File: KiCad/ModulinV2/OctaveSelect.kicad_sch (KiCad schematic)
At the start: 53 parts, among them IC21 SN74LV10ADR, IC22 SN74LV10ADR, IC23 SN74LV10ADR, IC24 SN74HC193DR, IC25 TMUX4051DYYRQ1, IC26 CD4028BM96, Q3 BC847B,215, Q4 BC847B,215, Q5 BC847B,215, Q6 BC847B,215, Q7 BC847B,215

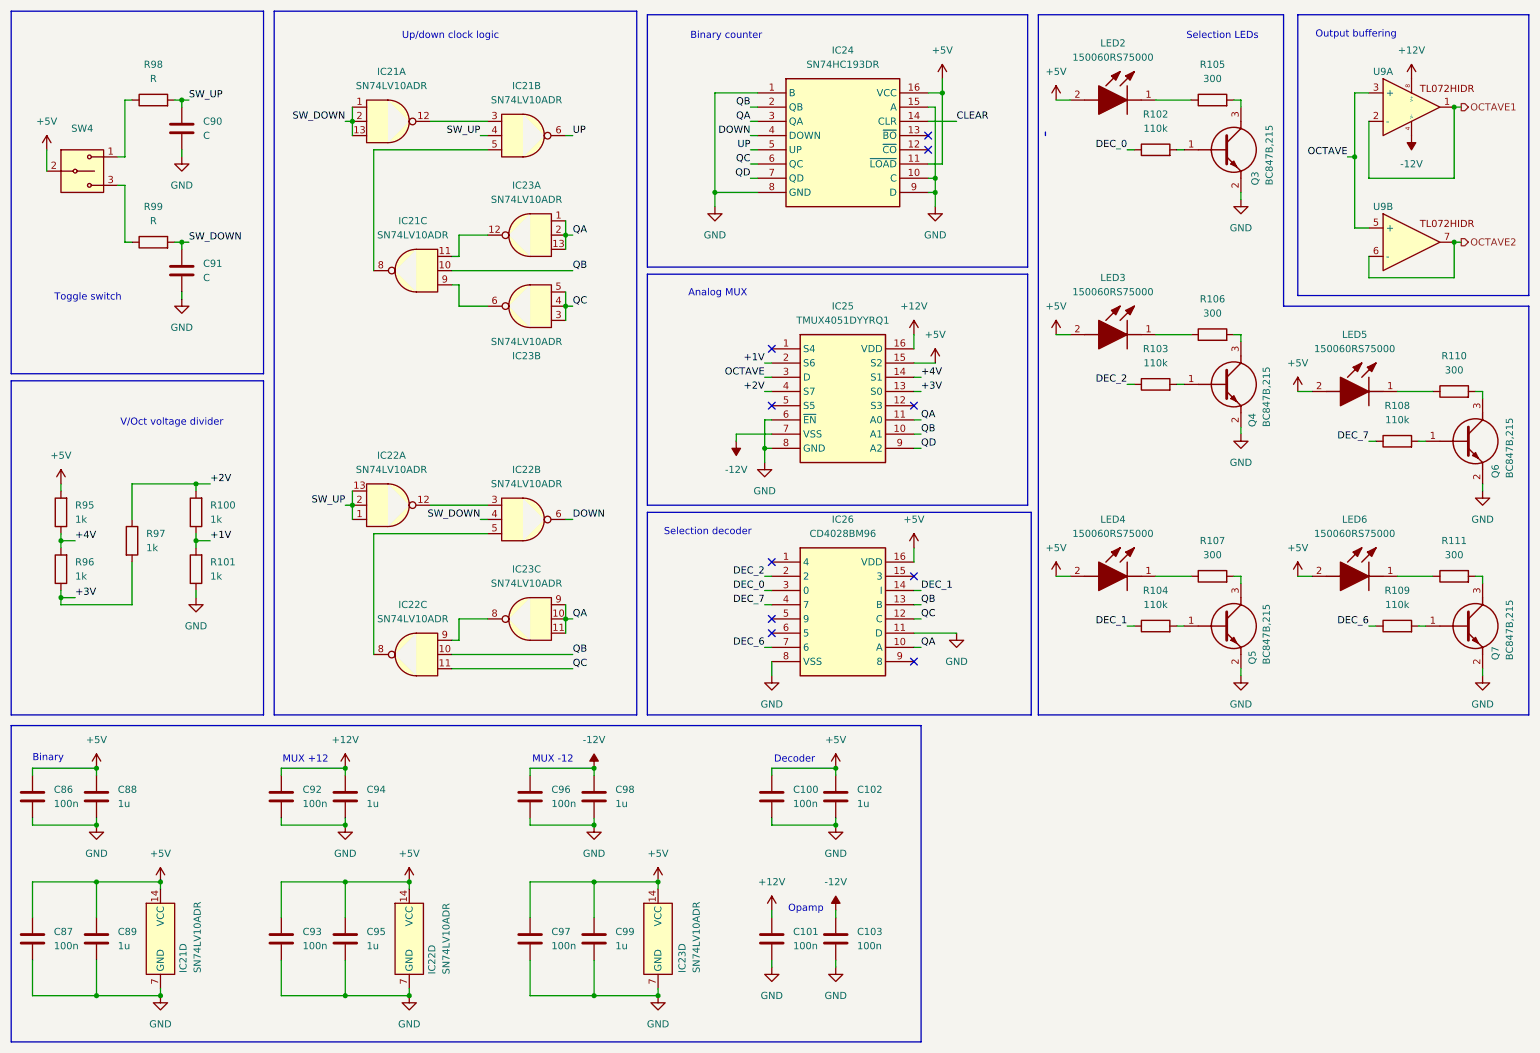
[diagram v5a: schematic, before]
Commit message: Added 4k7 pullups to I2C lines
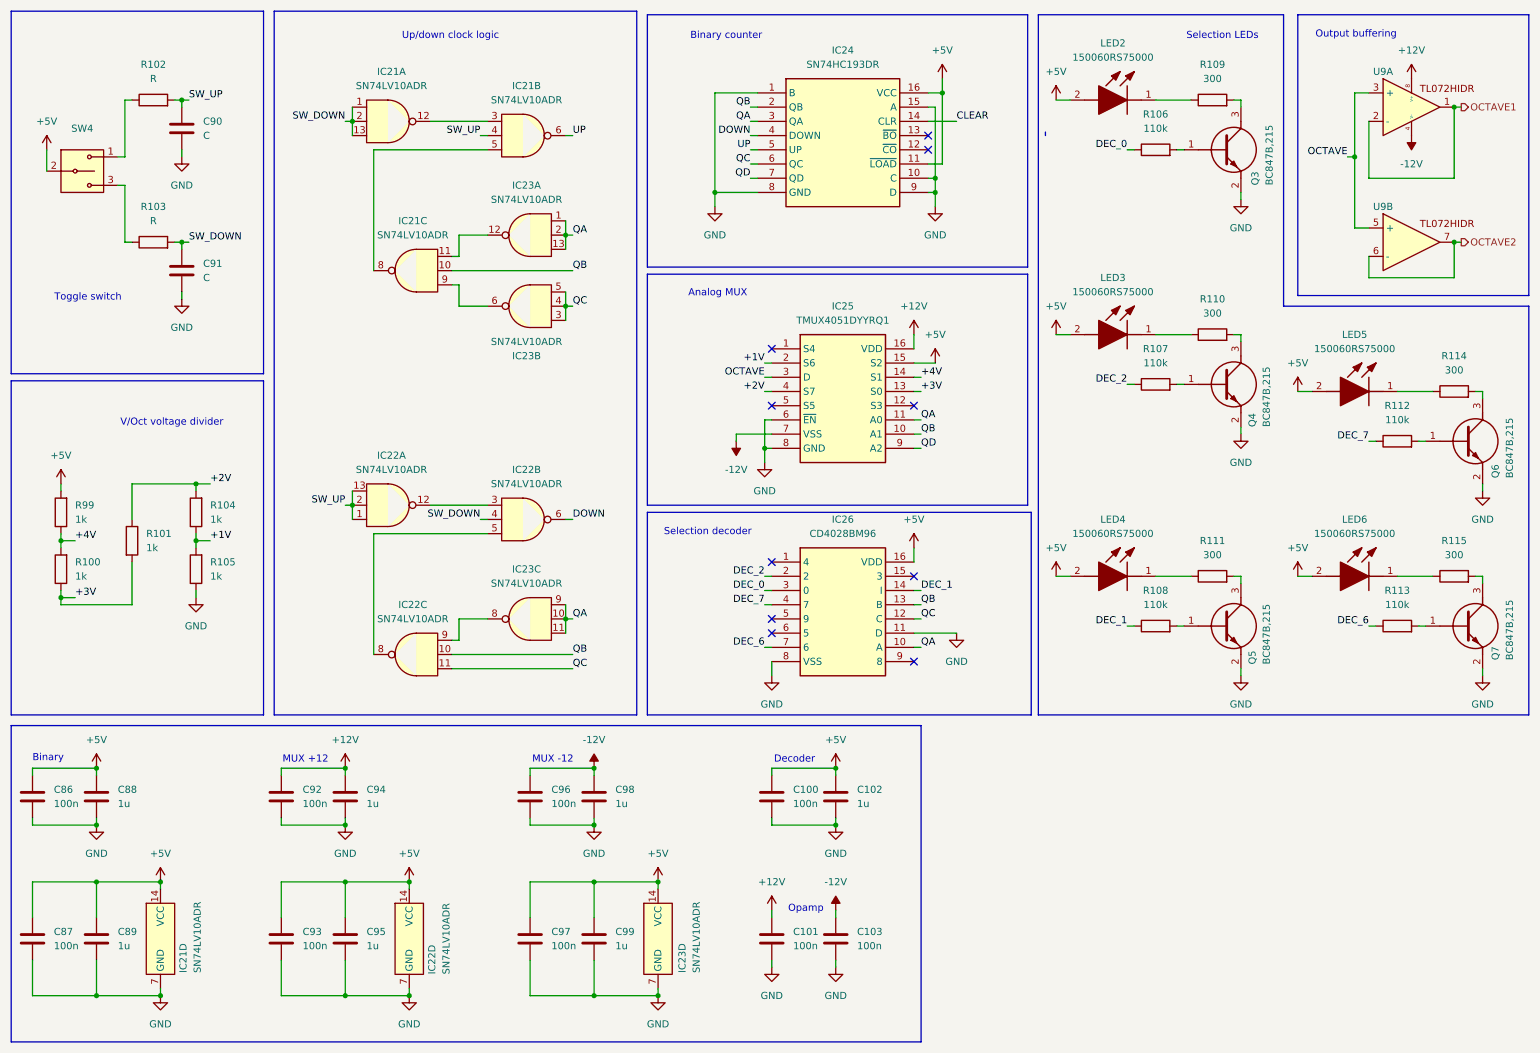
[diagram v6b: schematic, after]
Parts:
- renumbered R96 to R100, R97 to R101, R98 to R102, R99 to R103, R100 to R104, R101 to R105, R102 to R106, R103 to R107, R104 to R108, R105 to R109, R106 to R110, R107 to R111, R108 to R112, R109 to R113, R110 to R114, R111 to R115, R95 to R99

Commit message: Added wave selection jumpers for testing
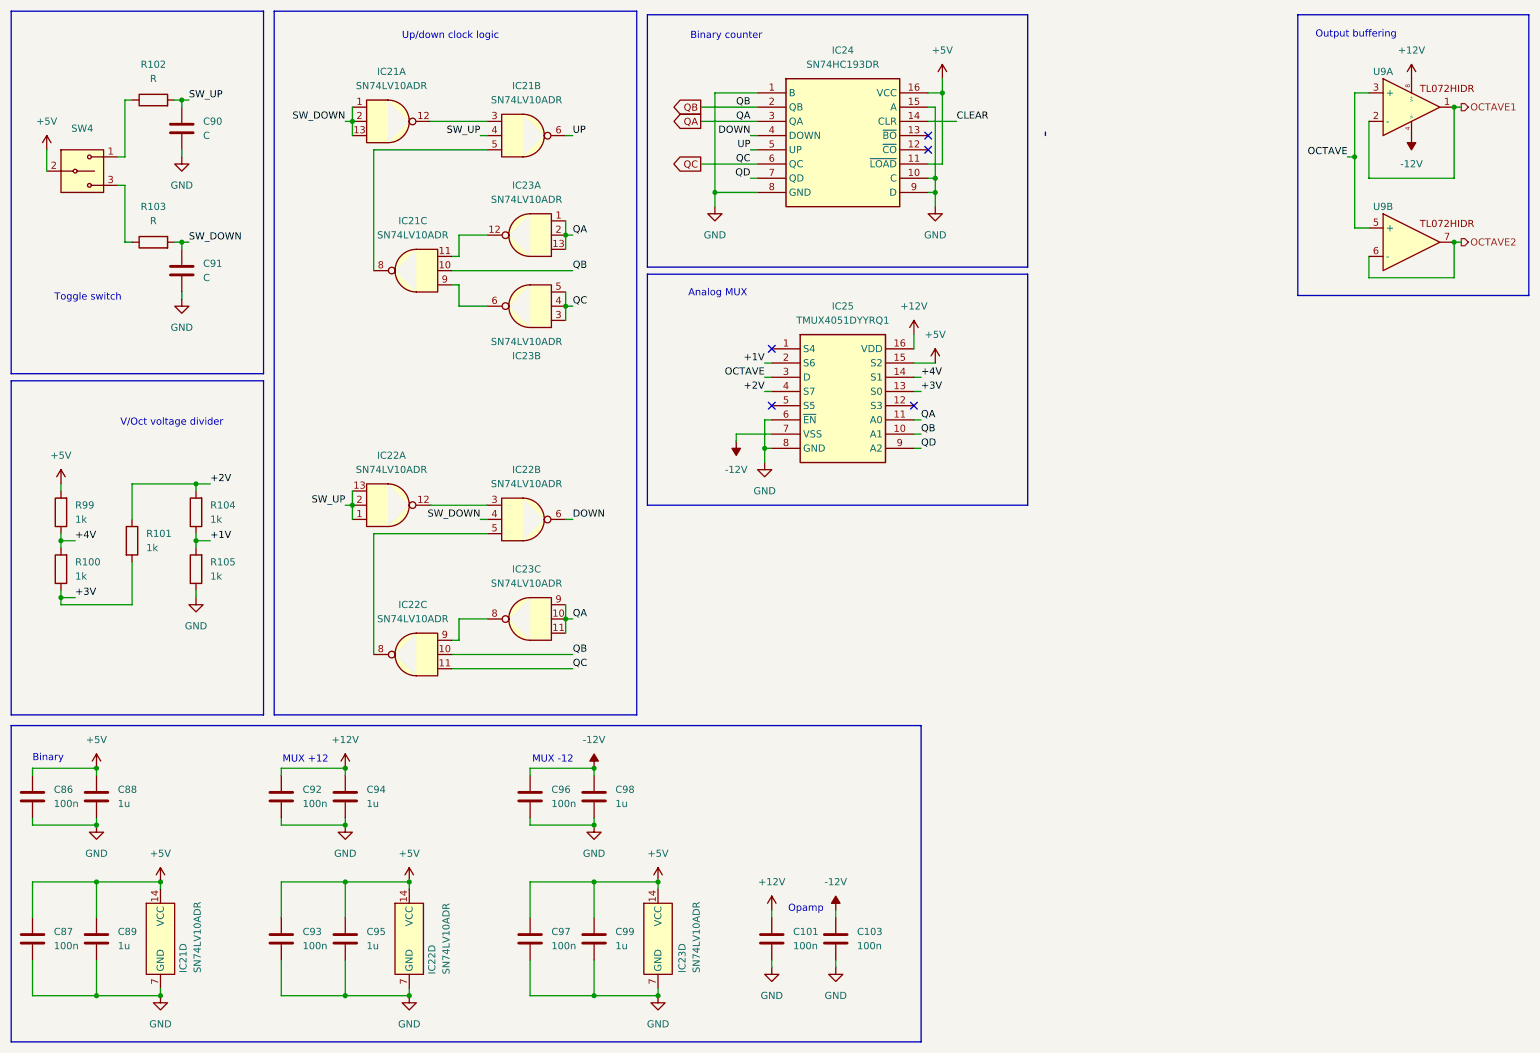
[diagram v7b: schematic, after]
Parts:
- removed C100: 100n, symbol Device:C
- removed C102: 1u, symbol Device:C
- removed IC26: CD4028BM96, SOIC127P600X175-16N, symbol CD4028BM96:CD4028BM96
- removed LED2, LED3, LED4, LED5, LED6: 150060RS75000, LEDC1608X80N, symbol 150060RS75000:150060RS75000
- removed Q3, Q4, Q5, Q6, Q7: BC847B,215, BC847B215, symbol BC847B_215:BC847B,215
- removed R106, R107, R108, R112, R113: 110k, symbol Device:R
- removed R109, R110, R111, R114, R115: 300, symbol Device:R
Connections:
- no-connect marks 10 -> 5
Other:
- note removed: "Decoder"
- note removed: "Selection LEDs"
- note removed: "Selection decoder"

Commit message: Revert "Modified selection LED schematic and supply caps"
This reverts commit f7ca9d31056dcb2cadf4048ae59e1f5625a2aefa.
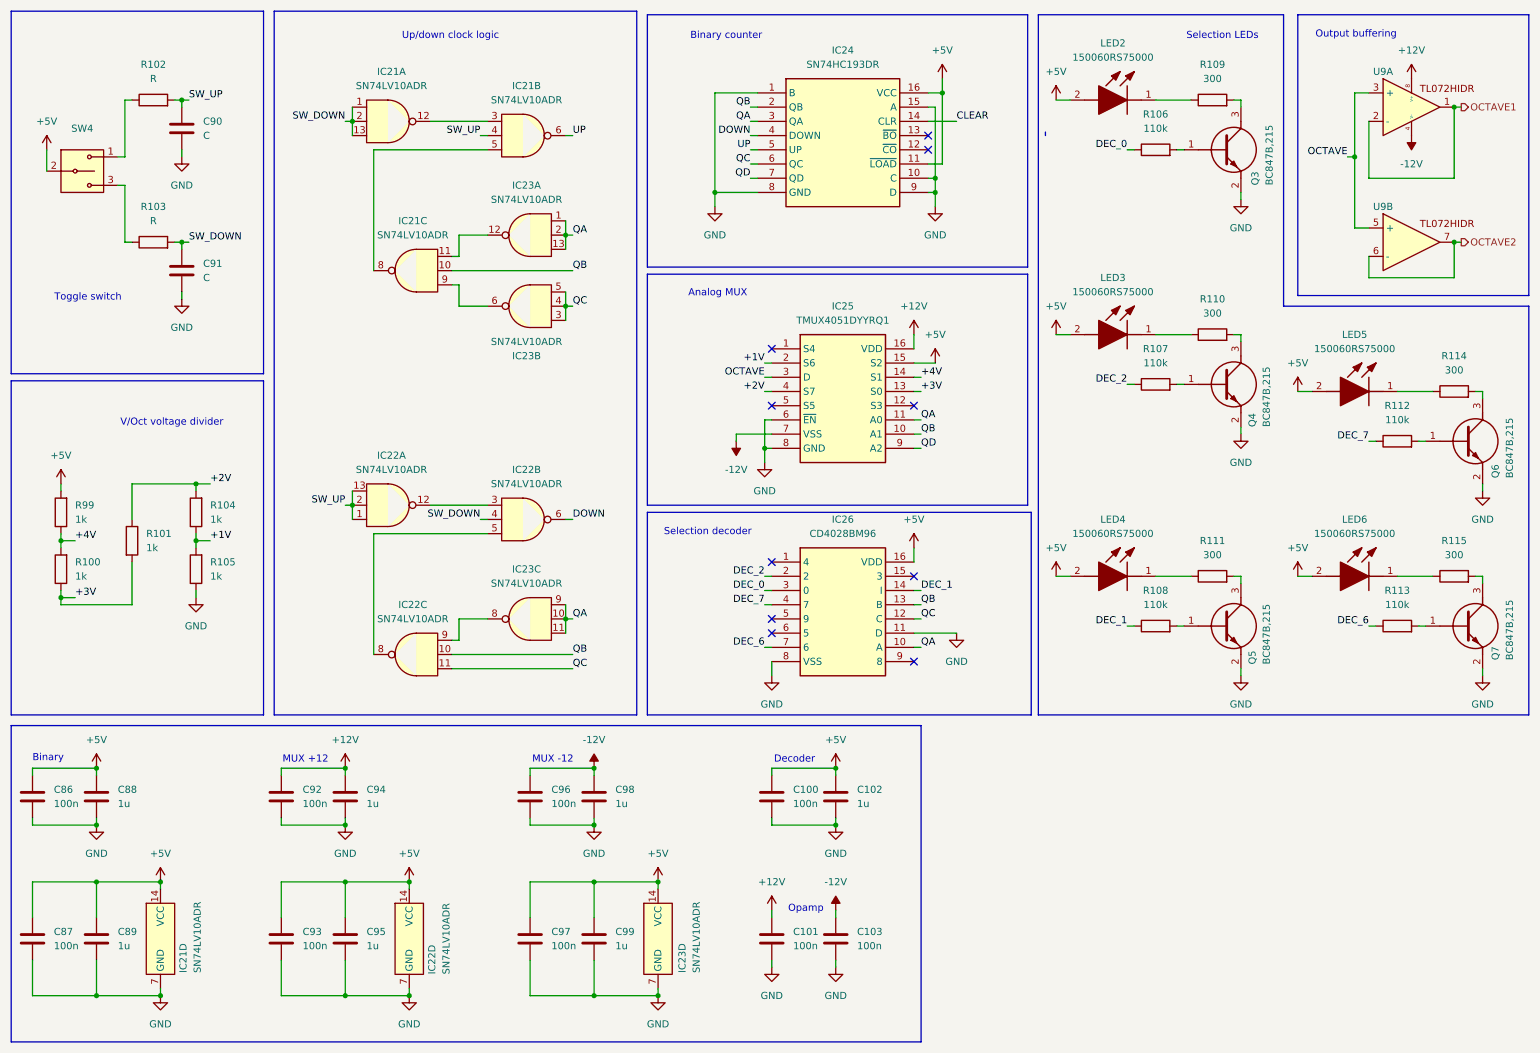
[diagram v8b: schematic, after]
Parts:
- added C100: 100n, symbol Device:C
- added C102: 1u, symbol Device:C
- added IC26: CD4028BM96, SOIC127P600X175-16N, symbol CD4028BM96:CD4028BM96
- added LED2, LED3, LED4, LED5, LED6: 150060RS75000, LEDC1608X80N, symbol 150060RS75000:150060RS75000
- added Q3, Q4, Q5, Q6, Q7: BC847B,215, BC847B215, symbol BC847B_215:BC847B,215
- added R106, R107, R108, R112, R113: 110k, symbol Device:R
- added R109, R110, R111, R114, R115: 300, symbol Device:R
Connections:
- net +5V: now also C100.2, C102.2, IC26.16 (VDD), LED2.2 (A), LED3.2 (A), LED4.2 (A), LED5.2 (A), LED6.2 (A)
- net GND: now also C100.1, C102.1, IC26.11 (D), IC26.8 (VSS), Q3.2 (E), Q4.2 (E), Q5.2 (E), Q6.2 (E), Q7.2 (E)
- net QA: now also IC26.10 (A)
- net QB: now also IC26.13 (B)
- net QC: now also IC26.12 (C)
- new net: LED5.1 (K), R114.1
- new net: LED2.1 (K), R109.1
- new net: Q3.3 (C), R109.2
- new net: Q7.1 (B), R113.2
- new net: Q5.1 (B), R108.2
- new net: Q5.3 (C), R111.2
- new net: LED4.1 (K), R111.1
- new net: Q4.1 (B), R107.2
- new net: Q4.3 (C), R110.2
- new net: LED6.1 (K), R115.1
- new net: Q7.3 (C), R115.2
- new net: LED3.1 (K), R110.1
- new net: Q6.1 (B), R112.2
- new net: Q6.3 (C), R114.2
- new net: Q3.1 (B), R106.2
- new net DEC_0: IC26.3 (0), R106.1
- new net DEC_1: IC26.14 (I), R108.1
- new net DEC_2: IC26.2, R107.1
- new net DEC_6: IC26.7 (6), R113.1
- new net DEC_7: IC26.4 (7), R112.1
- no-connect marks 5 -> 10
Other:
- note added: "Decoder"
- note added: "Selection LEDs"
- note added: "Selection decoder"
